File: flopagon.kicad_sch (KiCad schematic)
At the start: 17 parts, among them J1 Hexpansion-Connector, U1 M24C01-RMN, U2 W25Q128JVSIQ

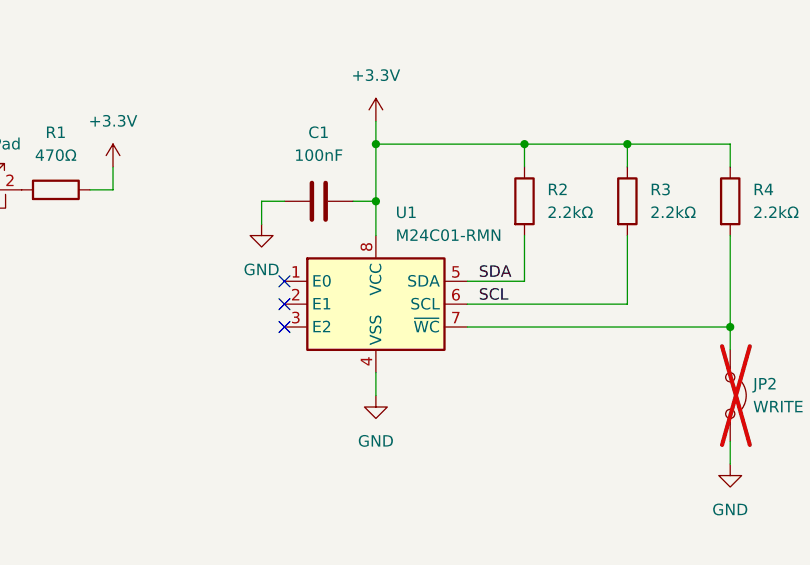
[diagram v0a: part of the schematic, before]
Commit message: Updated schematic to make the EEPROM part clearer
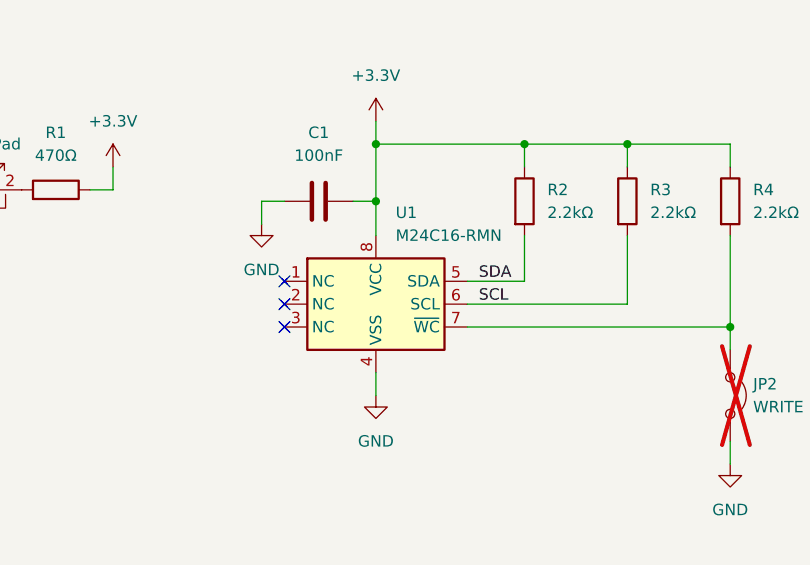
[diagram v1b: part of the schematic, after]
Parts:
- U1: value M24C01-RMN -> M24C16-RMN; symbol Memory_EEPROM:M24C01-RMN -> extras:M24C16-RMN
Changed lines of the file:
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@@
 	(label "GND"
 		(at 69.85 118.11 180)
-		(fields_autoplaced yes)
 		(effects
 			(font
@@
 	(label "SCL"
 		(at 71.12 64.77 180)
-		(fields_autoplaced yes)
 		(effects
 			(font
@@
 	(label "SDA"
 		(at 71.12 62.23 180)
-		(fields_autoplaced yes)
 		(effects
 			(font
@@
 	(label "HS_I"
 		(at 96.52 85.09 0)
-		(fields_autoplaced yes)
 		(effects
 			(font
@@
 	(label "HS_F"
 		(at 147.32 36.83 180)
-		(fields_autoplaced yes)
 		(effects
 			(font
@@
 	(label "HS_H"
 		(at 147.32 41.91 180)
-		(fields_autoplaced yes)
 		(effects
 			(font
@@
 	(label "~{HOLD}"
 		(at 142.24 49.53 0)
-		(fields_autoplaced yes)
 		(effects
 			(font
@@
 	(label "HS_F"
 		(at 96.52 77.47 0)
-		(fields_autoplaced yes)
 		(effects
 			(font
@@
 	(label "HS_G"
 		(at 96.52 80.01 0)
-		(fields_autoplaced yes)
 		(effects
 			(font
@@
 	(label "HS_H"
 		(at 96.52 82.55 0)
-		(fields_autoplaced yes)
 		(effects
 			(font
@@
 	(label "SCL"
 		(at 243.84 49.53 0)
-		(fields_autoplaced yes)
 		(effects
 			(font
@@
 	(label "~{WP}"
 		(at 142.24 46.99 0)
-		(fields_autoplaced yes)
 		(effects
 			(font
@@
 	(label "HS_I"
 		(at 147.32 44.45 180)
-		(fields_autoplaced yes)
 		(effects
 			(font
@@
 	(label "SDA"
 		(at 243.84 46.99 0)
-		(fields_autoplaced yes)
 		(effects
 			(font
@@
 	(label "HS_G"
 		(at 147.32 39.37 180)
-		(fields_autoplaced yes)
 		(effects
 			(font
@@
 	)
 	(symbol
-		(lib_id "Memory_EEPROM:M24C01-RMN")
+		(lib_id "extras:M24C16-RMN")
 		(at 232.41 49.53 0)
 		(unit 1)
@@
 			)
 		)
-		(property "Value" "M24C01-RMN"
+		(property "Value" "M24C16-RMN"
 			(at 234.6041 41.91 0)
 			(effects
@@
 			)
 		)
-		(property "Description" "1Kb (128x8) I2C Serial EEPROM, 1.8-5.5V, SOIC-8"
+		(property "Description" "16Kb (2048x8) I2C Serial EEPROM, 2.5-5.5V, SOIC-8"
 			(at 232.41 49.53 0)
 			(effects
